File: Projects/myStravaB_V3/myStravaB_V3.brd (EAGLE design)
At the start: 52.3 x 77.5 mm, 85 parts, among them IC1 TPS63051RMWT, IC2 BMD-340-A-R, IC3 BME280, Q2 BSS138BKW, T2 BC847, U1 FXOS8700CQR1, U2 MCP73831, U3 FM24CL16B, Y3 32.768kHz

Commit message: Simplified strava
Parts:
- removed BTNC1, BTND1, BTNG1: SKRMAAE010, SPST:SKRMAAE010
- removed C3, C5: 100nF, SparkFun-Capacitors:0603
- removed C38, C39: (no value), rcl:C0603
- removed C4: 10uF, SparkFun-Capacitors:0603
- removed D1: BAT54C, diode:SOT23
- removed L2: TBD, SparkFun-Resistors:0603
- removed R10, R25, R5, R8: 100k, rcl:R0603
- removed R11: 300k, rcl:R0603
- removed R20: 47, SparkFun-Resistors:0603
- removed R22: 80, SparkFun-Resistors:0603
- removed R26: 10k, rcl:R0603
- removed R9: 47k, rcl:R0603
- removed T2: BC847, nxp_60:SOT23
- removed U$1: DMG6602, nxp_60:TSOT26
- removed U$14: VEML6075, VEML6075:VEML6075
- removed U$17, U$18, U$19: KPA-2106SECK, KPA_LED:KPA-2106SECK
- removed U$7: PROG_SMD, Prog:PROG_SMD
- added B1: MICRO-SD_FOOTPRINT, SD_Card:MICRO-SD-FOOTPRINT
- added J1, SD: 47571-0001, SD_Card:47571-0001
- added M1, M2: (no value), MOSFET:SOT65P210X110-3N
- added SPST1, SPST2, SPST3: PTS526SK08, SPST:PTS526SKG15SMTR2LFS
- added U4: (no value), PowerSupplies:SOT753
- C1: value 1uF -> 4.7uF
- R3, R4: value 10k -> 100k
- moved C1 64.8 mm to (17.2, 30.5), turned to 90 degrees
- moved C17 62.3 mm to (-16.8, -31.1), turned to 0 degrees
- moved C7 61.5 mm to (-5.53, -32.6), turned to 180 degrees
- moved C6 61.3 mm to (1.07, -28.7), turned to 180 degrees
- moved IC3 60.2 mm to (-15.6, -28.5), flipped to the bottom, turned to 270 degrees
- moved U1 58.7 mm to (-3.23, -29.2), turned to 0 degrees
- moved U3 57.9 mm to (13.0, -29.4), turned to 0 degrees
- moved C9 57.6 mm to (0.01, -26.2), turned to 90 degrees
- moved R31 56.8 mm to (12.4, -24.3), turned to 270 degrees
- moved C10 56.7 mm to (-16.7, -25.5), flipped to the bottom, turned to 0 degrees
- moved C8 55.4 mm to (-2.50, -26.1), turned to 180 degrees
- moved R30 47.1 mm to (14.5, -24.3)
- moved R4 34.2 mm to (19.6, 17.7)
- moved R3 23.5 mm to (10.6, -10.6), turned to 0 degrees
- moved U$2 5.46 mm to (-10.2, 8.18)
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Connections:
- removed net BCK_LED_TR: R20.2, U$19.P$1, U$6.IO
- removed net INT1: IC2.9, U1.11
- removed net INT2: U1.9
- removed net INT_PSWITCH: D1.2, R10.2, R11.1, T2.3
- removed net INV: C1.1, C3.1, R5.1, R8.1, U$1.P$6
- removed net KILL_NRF: IC2.28, R25.2, R26.2
- removed net N$12: R25.1, T2.1
- removed net N$15: C4.1, R11.2, U$1.P$1
- removed net N$16: R22.2, U$19.P$2
- removed net N$17: R20.1, U$17.P$1, U$18.P$1
- removed net N$3: R5.2, U$1.P$3
- removed net NRF_BTNC: C5.2, D1.1, IC2.31, R9.1
- removed net PW_EN: C4.2, IC1.11, L4.1-VDD, R10.1, R14.1, R18.2, R4.1, U$1.P$4
- removed net RF_IN: C38.1, L2.2, U$5.P$3
- new net 5V: L4.1-VDD, R18.2, U$16.6, U$16.7, U4.5
- new net FXOS_INT1: IC2.58, U1.11
- new net POW_EN: IC1.11, M2.3, R14.1, U4.3
- new net SD_CLK: IC2.8, SD.25
- new net SD_CS: IC2.7, SD.22
- new net SD_MISO: IC2.9, SD.27
- new net SD_MOSI: IC2.6, SD.23
- new net SWON: M2.1, R3.1, U$6.IO
- net ANT: now also U$5.P$3; no longer C39.1, L2.1
- net BTNC: now also IC2.31, SPST2.3, SPST2.4; no longer BTNC1.P$2, BTNC1.P$4, C1.2, D1.3, R3.1
- net BTND: now also SPST3.3, SPST3.4; no longer BTND1.P$2, BTND1.P$4
- net BTNG: now also SPST1.3, SPST1.4; no longer BTNG1.P$2, BTNG1.P$4
- net FXOS_RST: now also IC2.59; no longer IC2.8
- net GND: now also C1.1, J1.10, J1.11, J1.12, J1.13, J1.26, J1.9, R4.2, SD.26, SPST1.1, SPST1.2, SPST2.1, SPST2.2, SPST3.1, SPST3.2, U4.2; no longer BTNC1.P$1, BTNC1.P$3, BTND1.P$1, BTND1.P$3, BTNG1.P$1, BTNG1.P$3, C3.2, C38.2, C39.2, C5.1, R26.1, T2.2, U$1.P$5, U$14.P$1, U$7.GND
- net SCL: now also IC2.57; no longer IC2.6, U$14.P$3
- net SDA: now also IC2.56; no longer IC2.7, U$14.P$2
- net SWDCLK: now also J1.21; no longer U$7.PIN1
- net SWDIO: now also J1.28; no longer U$7.PIN2
- net VBAT: now also M1.3, M2.2; no longer D3.2, R8.2, U$1.P$2
- net VCC: now also C1.2, J1.24, SD.24; no longer R22.1, R9.2, U$14.P$4, U$16.6, U$16.7, U$17.P$2, U$18.P$2, U$7.VCC
- net VIN: now also M1.2, U4.1
- net VUSB: now also M1.1, R4.1; no longer R4.2
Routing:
- net 5V: track 0.00 -> 105.3 mm, vias 0 -> 4
- net PW_EN: track 103.1 -> 0.00 mm, vias 2 -> 0
- net BCK_LED_TR: track 98.5 -> 0.00 mm, vias 3 -> 0
- net VCC: track 130.2 -> 207.3 mm, vias 36 -> 17
- net KILL_NRF: track 66.7 -> 0.00 mm, vias 2 -> 0
- net NRF_BTNC: track 59.7 -> 0.00 mm, vias 2 -> 0
- net FXOS_INT1: track 0.00 -> 54.9 mm, vias 0 -> 2
- net BTNC: track 23.3 -> 73.2 mm, vias 1 -> 3
- net SD_MISO: track 0.00 -> 32.1 mm
- net SD_CLK: track 0.00 -> 32.0 mm
- net INT1: track 31.4 -> 0.00 mm
- net SD_MOSI: track 0.00 -> 30.6 mm
- net SD_CS: track 0.00 -> 27.5 mm
- net FXOS_RST: track 29.6 -> 56.6 mm, vias 0 -> 2
- net POW_EN: track 0.00 -> 23.7 mm, vias 0 -> 2
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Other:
- outline, holes or cut-outs redrawn

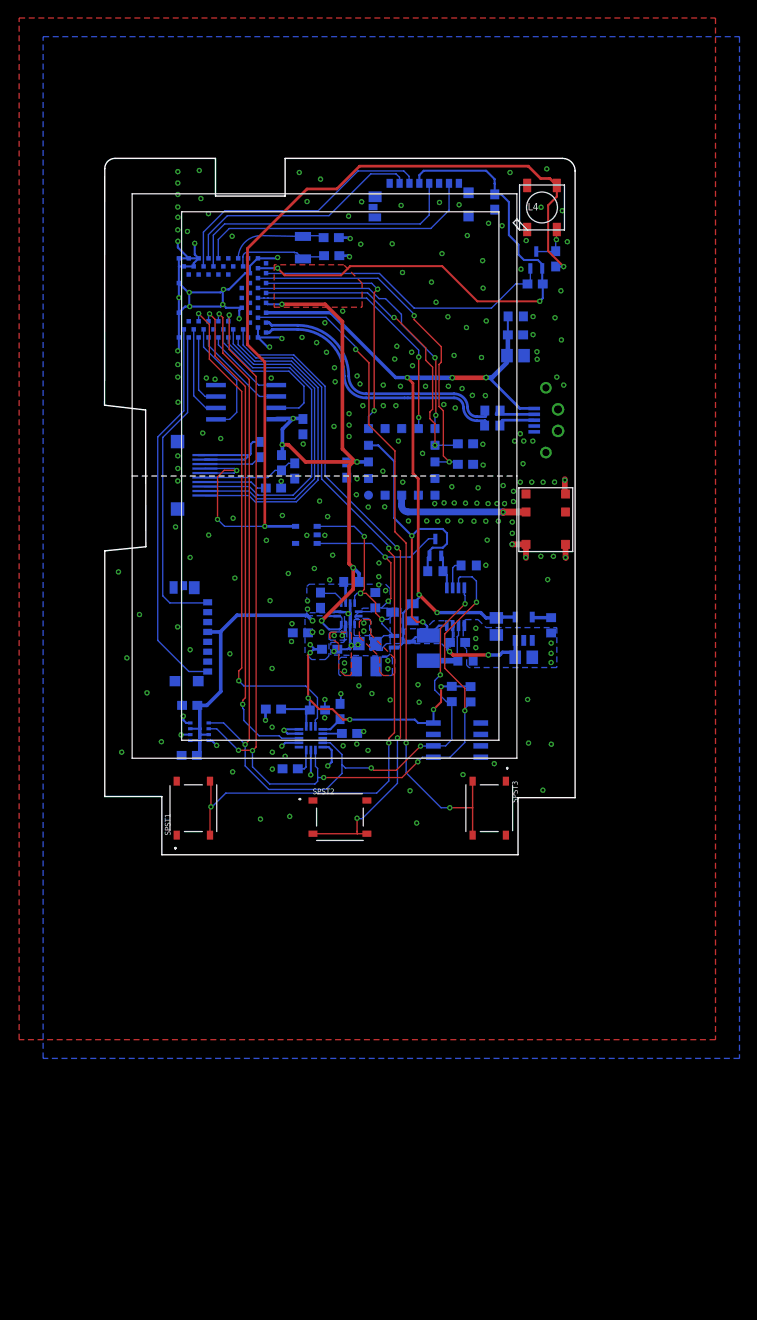
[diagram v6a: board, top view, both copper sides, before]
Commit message: Updated 5V boost DCDC converter
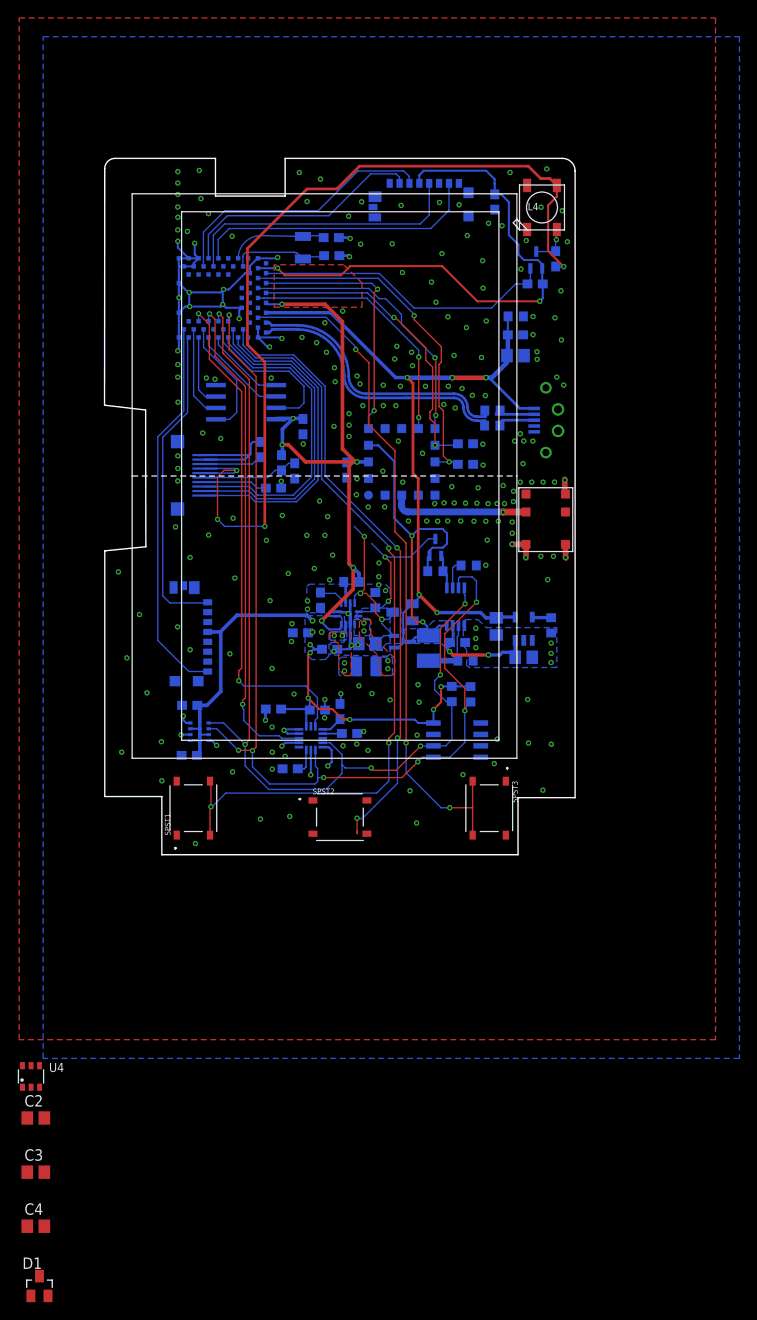
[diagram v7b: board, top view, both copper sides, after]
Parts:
- added C2, C3: 10uF, rcl:C0805
- added C4: 220nF, rcl:C0805
- added D1: BAT54C, diode:SOT23
- U4: value (none) -> REG710; device PowerSupplies:SOT753 -> DCDC:SOT457
- moved U4 67.6 mm to (-34.4, -66.8), flipped to the top, turned to 0 degrees
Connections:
- new net BTNC_HV: D1.3, SPST2.3, SPST2.4
- new net N$5: C4.1, U4.6
- new net N$6: C4.2, U4.4
- net 5V: now also C3.2, U4.1; no longer U4.5
- net BTNC: now also D1.1; no longer SPST2.3, SPST2.4
- net GND: now also C2.1, C3.1
- net SWON: now also D1.2
- net VIN: now also C2.2, U4.5; no longer U4.1
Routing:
- net POW_EN: track 23.7 -> 17.6 mm
- net BTNC: track 73.2 -> 67.2 mm
- net VIN: track 24.5 -> 20.4 mm
- net 5V: track 105.3 -> 101.9 mm
- net GND: vias 237 -> 242

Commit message: Updated stravaV3 Updated Climber
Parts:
- IC1: device SamacSys_Parts:QFN50P250X250X100-12N -> DCDC:QFN50P250X250X100-12N
- moved C4 76.0 mm to (-7.62, -12.2), flipped to the bottom, turned to 180 degrees
- moved C3 72.3 mm to (-10.7, -8.97), flipped to the bottom, turned to 90 degrees
- moved C2 69.1 mm to (-3.96, -9.09), flipped to the bottom
- moved D1 65.7 mm to (6.53, -38.0), flipped to the bottom, turned to 180 degrees
- moved U4 63.7 mm to (-7.62, -9.07), flipped to the bottom, turned to 180 degrees
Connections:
- net SCL: now also J1.23
- net SDA: now also J1.22
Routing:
- net SWON: track 3.82 -> 30.1 mm, vias 0 -> 2
- net POW_EN: track 17.6 -> 29.3 mm
- net VIN: track 20.4 -> 30.6 mm
- net BTNC_HV: track 0.00 -> 9.86 mm, vias 0 -> 1
- net SDA: track 112.9 -> 119.1 mm, vias 7 -> 8
- net SCL: track 108.5 -> 114.2 mm, vias 6 -> 7
- net BTNC: track 67.2 -> 62.3 mm, vias 3 -> 2
- net 5V: track 101.9 -> 106.4 mm
- net N$6: track 0.00 -> 1.92 mm
- net N$5: track 0.00 -> 1.92 mm
- net BTND: track 77.1 -> 78.0 mm
